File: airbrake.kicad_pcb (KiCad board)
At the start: 2 copper layers, 53.2 x 52.2 mm, 74 parts, among them IC1 SN74HCT125DR, J1 Molex Microfit, J2 Molex Microfit, J3 Molex Microfit, J4 Molex Microfit, J5 Molex Microfit, J6 Conn_02x03_Counter_Clockwise, U1 MS5607-02BA, U2 MMC5983MA, U3 STM32G431RBTx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

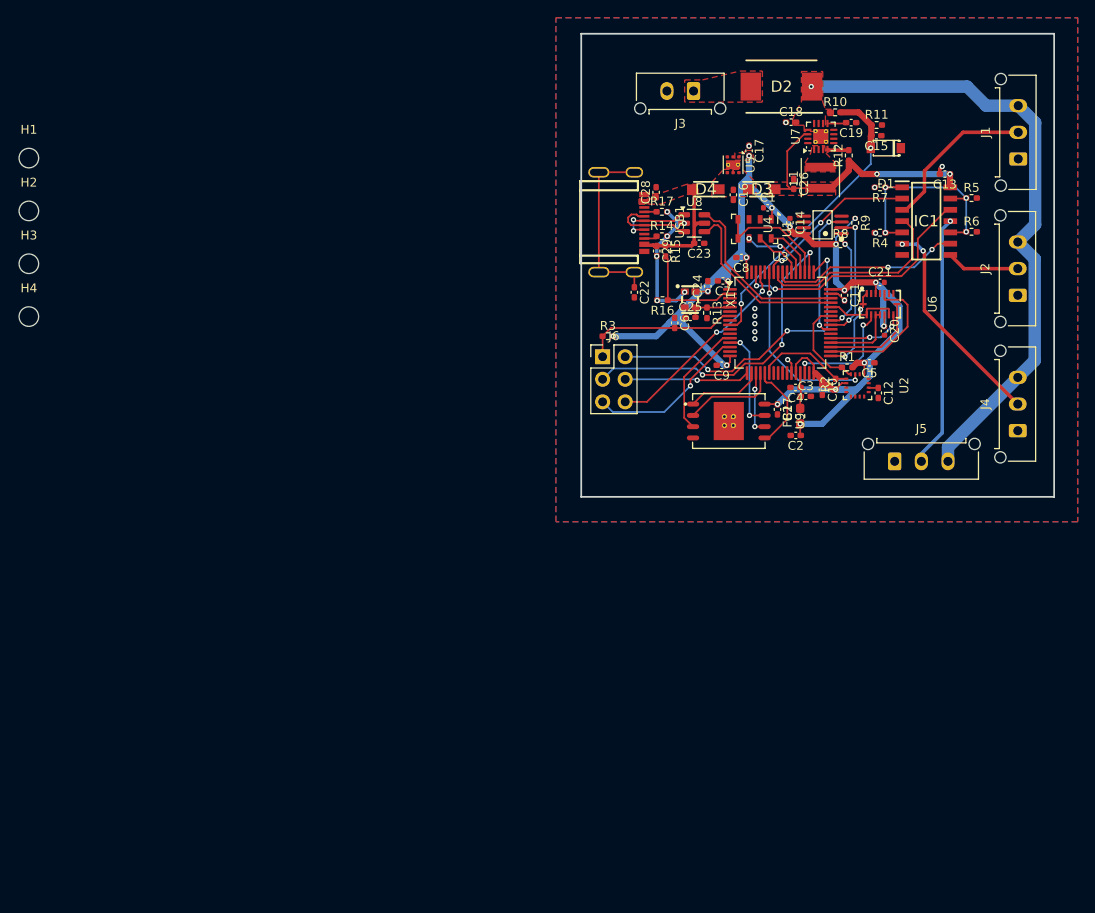
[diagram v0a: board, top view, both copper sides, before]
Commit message: Completed trace routing
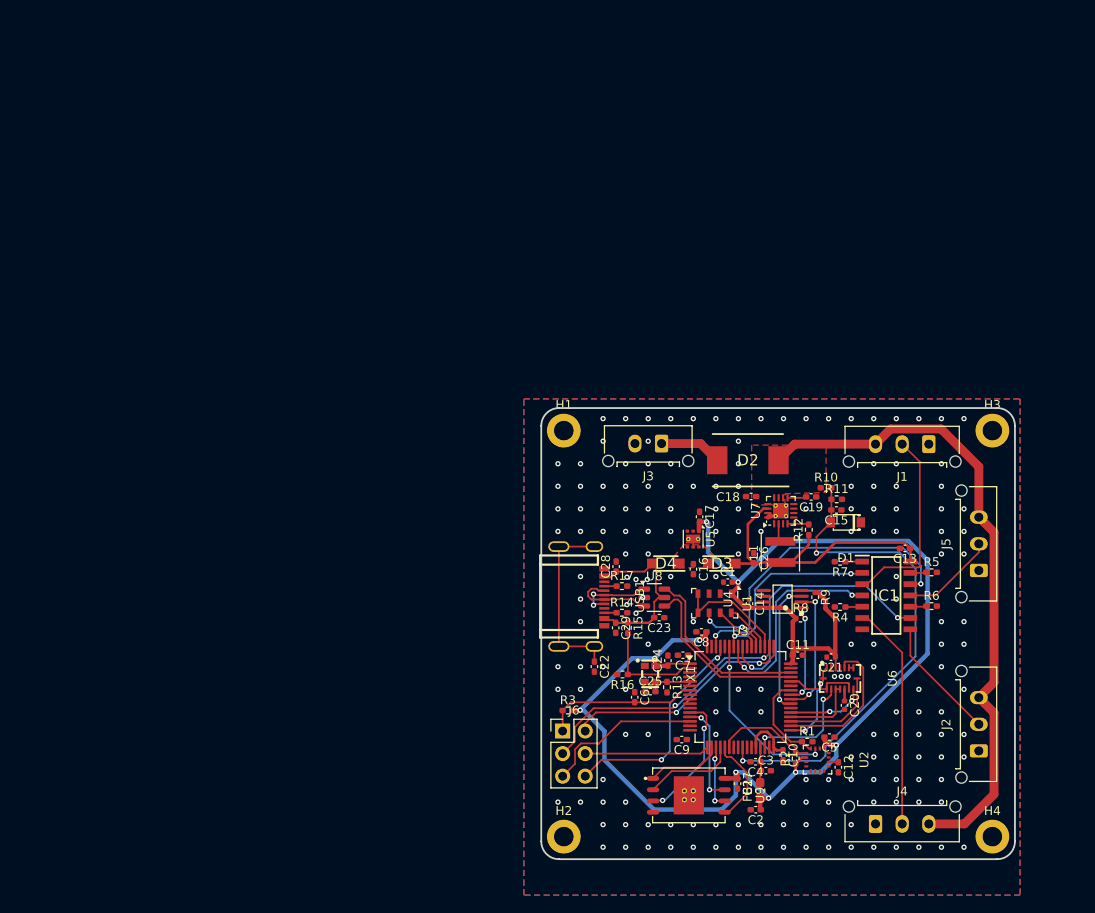
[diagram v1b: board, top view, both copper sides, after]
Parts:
- H1, H2, H3, H4: footprint MountingHole:MountingHole_2.2mm_M2 -> MountingHole:MountingHole_2.2mm_M2_DIN965_Pad
- moved H4 123.3 mm to (152.4, 124.5)
- moved H3 110.1 mm to (152.4, 78.7)
- moved H2 92.7 mm to (104.1, 124.5)
- moved H1 67.6 mm to (104.1, 78.7)
- moved J2 51.5 mm to (150.9, 114.8)
- moved J4 47.1 mm to (139.2, 123.0), turned to 0 degrees
- moved C14 43.1 mm to (125.0, 98.2)
- moved C29 42.7 mm to (110.0, 101.0)
- moved R15 42.6 mm to (111.3, 100.9)
- moved R14 42.6 mm to (110.7, 99.2)
- moved C21 42.6 mm to (134.2, 104.2), turned to 180 degrees
- moved C12 42.4 mm to (135.1, 116.7)
- moved C16 42.4 mm to (118.7, 94.3)
- moved C2 42.4 mm to (125.8, 121.4)
- moved C20 42.4 mm to (135.8, 109.7)
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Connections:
- U3 pad 25: unconnected-(U3-PB1-Pad25) -> BAT_LEVEL
- U3 pad 9: BAT_LEVEL -> unconnected-(U3-PC1-Pad9)
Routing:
- net BAT_LEVEL: track 33.6 -> 56.4 mm
- net VBAT-: track 21.5 -> 2.33 mm, vias 18 -> 179
- net /PWM_PD: track 25.7 -> 7.43 mm, vias 4 -> 0
- net SERVO_D: track 28.4 -> 10.7 mm, vias 1 -> 0
- net +3.3V: track 161.7 -> 177.8 mm, vias 17 -> 9
- net SWDIO: track 35.2 -> 26.5 mm, vias 3 -> 2
- net PWM_C: track 21.6 -> 30.2 mm
- net VBUS: track 15.8 -> 24.4 mm
- net PWM_D: track 28.2 -> 35.3 mm
- net Net-(D2-A): track 0.00 -> 7.04 mm
- net SWCLK: track 36.3 -> 29.9 mm, vias 3 -> 2
- net SERVO_C: track 8.23 -> 13.9 mm
- net +5V: track 30.3 -> 35.2 mm, vias 2 -> 0
- net SERVO_A: track 17.6 -> 21.9 mm
- net VBAT+: track 70.7 -> 73.5 mm, vias 1 -> 0
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- removed copper zone on F.Cu, net +3.3V
- removed copper zone on F.Cu, net +5V
- removed copper zone on F.Cu, net Net-(D2-A)
- removed copper zone on F.Cu, net Net-(L1-Pad2)
- removed copper zone on F.Cu, net VBUS
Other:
- board size 53.2 x 52.2 mm -> 53.3 x 50.8 mm

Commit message: minor fix
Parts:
- moved H3 0.90 mm to (151.8, 79.4)
- moved H1 0.90 mm to (104.8, 79.4)
- moved H4 0.90 mm to (151.8, 123.8)
- moved H2 0.90 mm to (104.8, 123.8)
- moved C27 0.13 mm to (123.6, 118.5)
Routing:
- net VBAT-: track 2.33 -> 4.95 mm
- net W25Q_MOSI: track 9.99 -> 9.30 mm

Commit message: Minor fix 2
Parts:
- moved C8 0.26 mm to (119.4, 101.4)
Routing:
- net VBAT-: track 4.95 -> 9.25 mm, vias 179 -> 181
